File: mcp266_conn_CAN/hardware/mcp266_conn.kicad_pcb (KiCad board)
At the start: 2 copper layers, 83.2 x 40.5 mm, 19 parts, among them J1 conn_dsub_plug_15pos, J10 CAN, J11 CANL jumper, J12 CANH jumper, J2 CAN, J3 LS1, J4 LS2, J5 LS3, J6 LS4, J7 Enc1, J8 Enc2, J9 enc conn

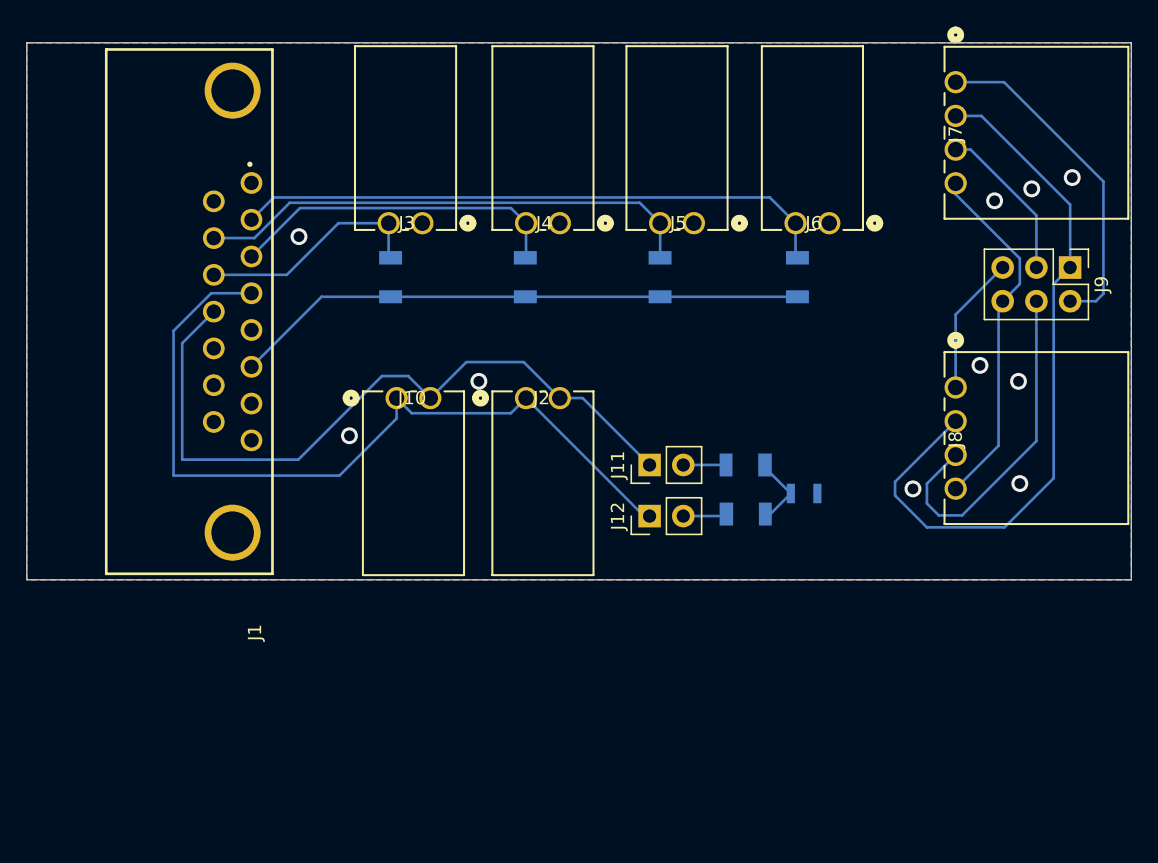
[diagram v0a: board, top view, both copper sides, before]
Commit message: design three seperate mcp connectors that can each dasiy chain for can, and one has limit switch headers and another the can termination
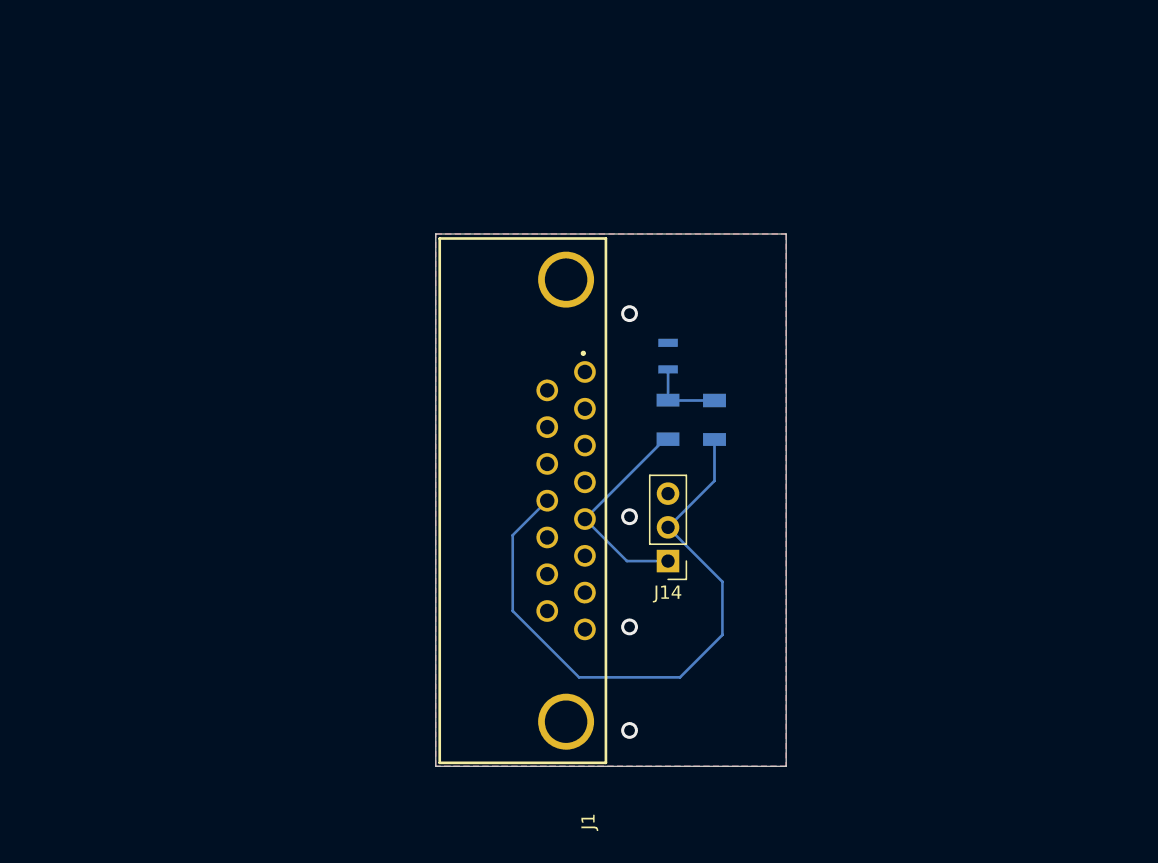
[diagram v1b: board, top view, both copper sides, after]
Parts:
- removed J10, J2: CAN, mcp266_conn:HEADER90_2pin
- removed J11: CANL jumper, Connector_PinHeader_2.54mm:PinHeader_1x02_P2.54mm_Vertical
- removed J12: CANH jumper, Connector_PinHeader_2.54mm:PinHeader_1x02_P2.54mm_Vertical
- removed J3: LS1, mcp266_conn:HEADER90_2pin
- removed J4: LS2, mcp266_conn:HEADER90_2pin
- removed J5: LS3, mcp266_conn:HEADER90_2pin
- removed J6: LS4, mcp266_conn:HEADER90_2pin
- removed J7: Enc1, mcp266_conn:HEADER90_4pin
- removed J8: Enc2, mcp266_conn:HEADER90_4pin
- removed J9: enc conn, Connector_PinHeader_2.54mm:PinHeader_2x03_P2.54mm_Vertical
- removed R2, R3, R4, R5: 5k, mcp266_conn:RESC3116X65N
- added J14: CAN, Connector_PinHeader_2.54mm:PinHeader_1x03_P2.54mm_Vertical, F.Cu at (127.9, 99.7)
- moved J1 28.9 mm to (113.9, 95.2)
- moved C1 14.6 mm to (127.9, 84.3), turned to -90 degrees
- moved R1 9.20 mm to (127.9, 89.1), turned to 90 degrees
- moved R6 4.13 mm to (131.4, 89.1), turned to -90 degrees
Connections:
- J1 pad 10: /LS3 -> unconnected-(J1-Pad10)
- J1 pad 11: /LS1 -> unconnected-(J1-Pad11)
- J1 pad 2: /LS4 -> GND
- J1 pad 3: /LS2 -> unconnected-(J1-Pad3)
- J1 pad 4: /CANH -> unconnected-(J1-Pad4)
- J1 pad 5: unconnected-(J1-Pad5) -> /CANH
- J1 pad 6: /5V -> unconnected-(J1-Pad6)
- J1 pad 7: GND -> unconnected-(J1-Pad7)
- R1 pad 1: /CANH_1 -> /CANH
- R6 pad 2: /CANL_L -> /CANL
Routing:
- net /5V_enc: track 54.5 -> 0.00 mm
- net /CANH: track 61.7 -> 16.3 mm
- net /LS4: track 44.8 -> 0.00 mm
- net /5V: track 43.4 -> 0.00 mm
- net /LS3: track 37.8 -> 0.00 mm
- net /GND_enc: track 27.0 -> 0.00 mm
- net /2B: track 26.0 -> 0.00 mm
- net /1A: track 25.4 -> 0.00 mm
- net /LS2: track 25.2 -> 0.00 mm
- net /LS1: track 17.4 -> 0.00 mm
- net /1B: track 12.1 -> 0.00 mm
- net /2A: track 10.5 -> 0.00 mm
- net /CANL: track 55.0 -> 46.5 mm
- net /CANH_1: track 3.31 -> 0.00 mm
- net /CANL_L: track 3.22 -> 0.00 mm
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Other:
- board size 83.2 x 40.5 mm -> 26.4 x 40.1 mm

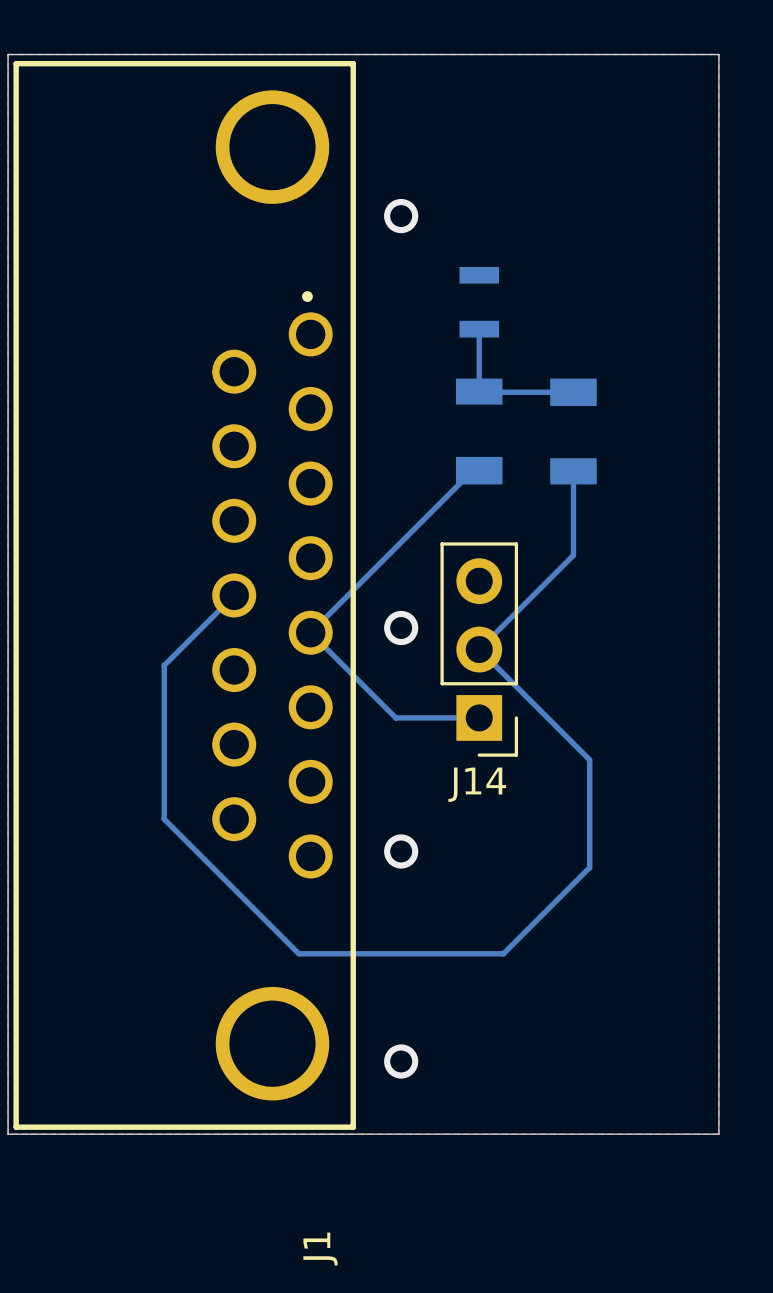
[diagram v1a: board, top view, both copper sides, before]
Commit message: made all in one mcp connector
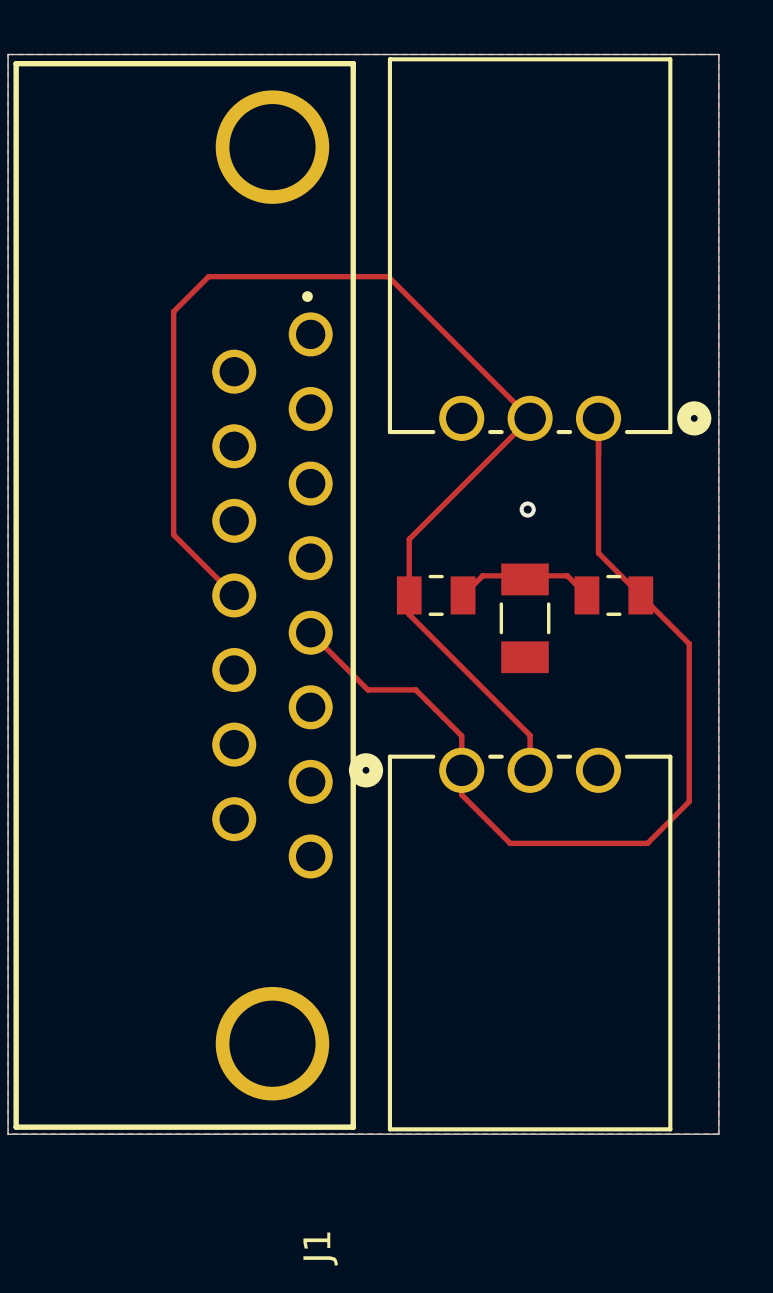
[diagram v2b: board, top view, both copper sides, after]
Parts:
- added J15: CAN, mcp266_conn:HEADER_3pos_90degree, F.Cu at (127.2, 101.7)
- C1: footprint mcp266_conn:CAPC2012X145N -> mcp266_conn:CAP_47nF; moved to F.Cu
- J14: footprint Connector_PinHeader_2.54mm:PinHeader_1x03_P2.54mm_Vertical -> mcp266_conn:HEADER_3pos_90degree
- R1, R6: footprint mcp266_conn:RESC3116X65N -> mcp266_conn:RES_60.4ohms; moved to F.Cu
- moved J14 12.0 mm to (132.3, 88.6)
- moved C1 11.9 mm to (129.6, 96.0), turned to 90 degrees
- moved R6 7.94 mm to (126.3, 95.2), turned to 180 degrees
- moved R1 7.88 mm to (132.9, 95.2), turned to 180 degrees
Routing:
- net /CANH: track 16.3 -> 36.2 mm
- net /CANL: track 46.5 -> 44.2 mm
- net Net-(C1-Pad2): track 5.83 -> 5.20 mm
- net GND: vias 4 -> 1
